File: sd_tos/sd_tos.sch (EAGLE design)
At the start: 18 parts, among them IC1 MEGA16-A, IC3 74HCT595D

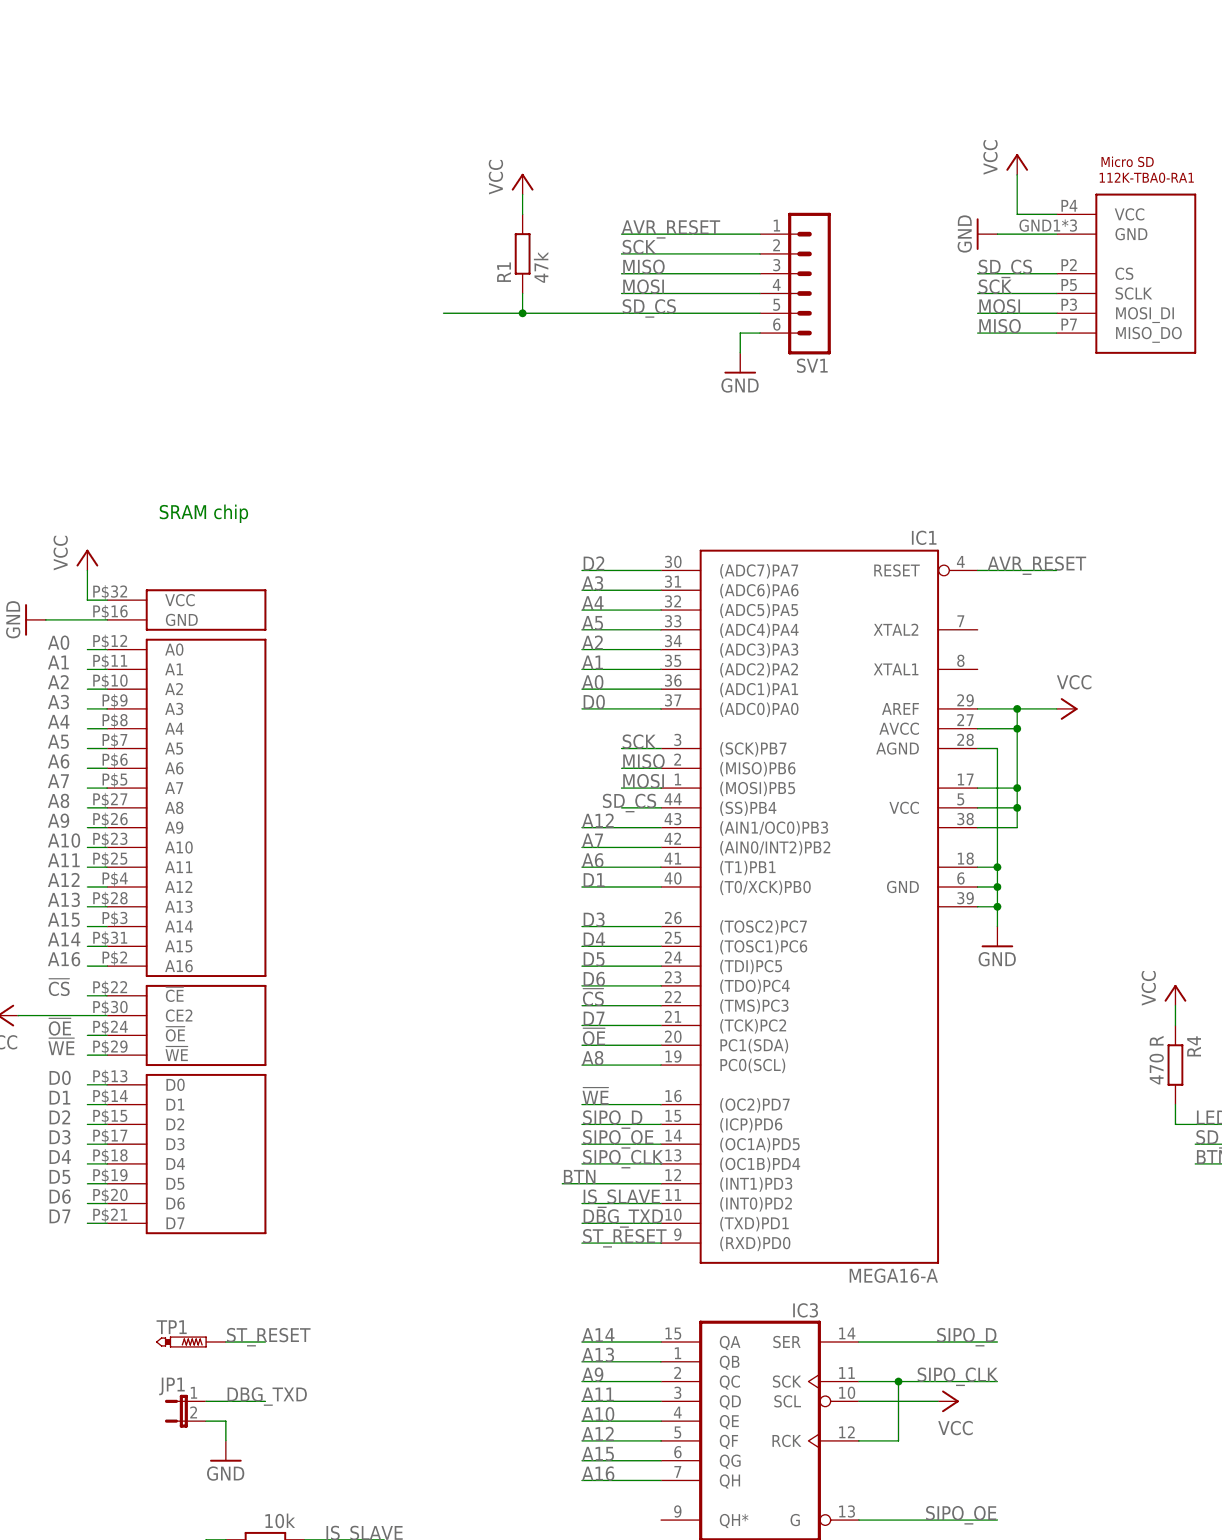
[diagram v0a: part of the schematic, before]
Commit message: added ST reset wire to master/slave connector, so you need to connect only single ST reset wire to the boards and they will share it
git-svn-id: https://subversion.assembla.com/svn/atarijookie/trunk@935 0d2ca917-fb58-4453-bb26-a698c01b0940
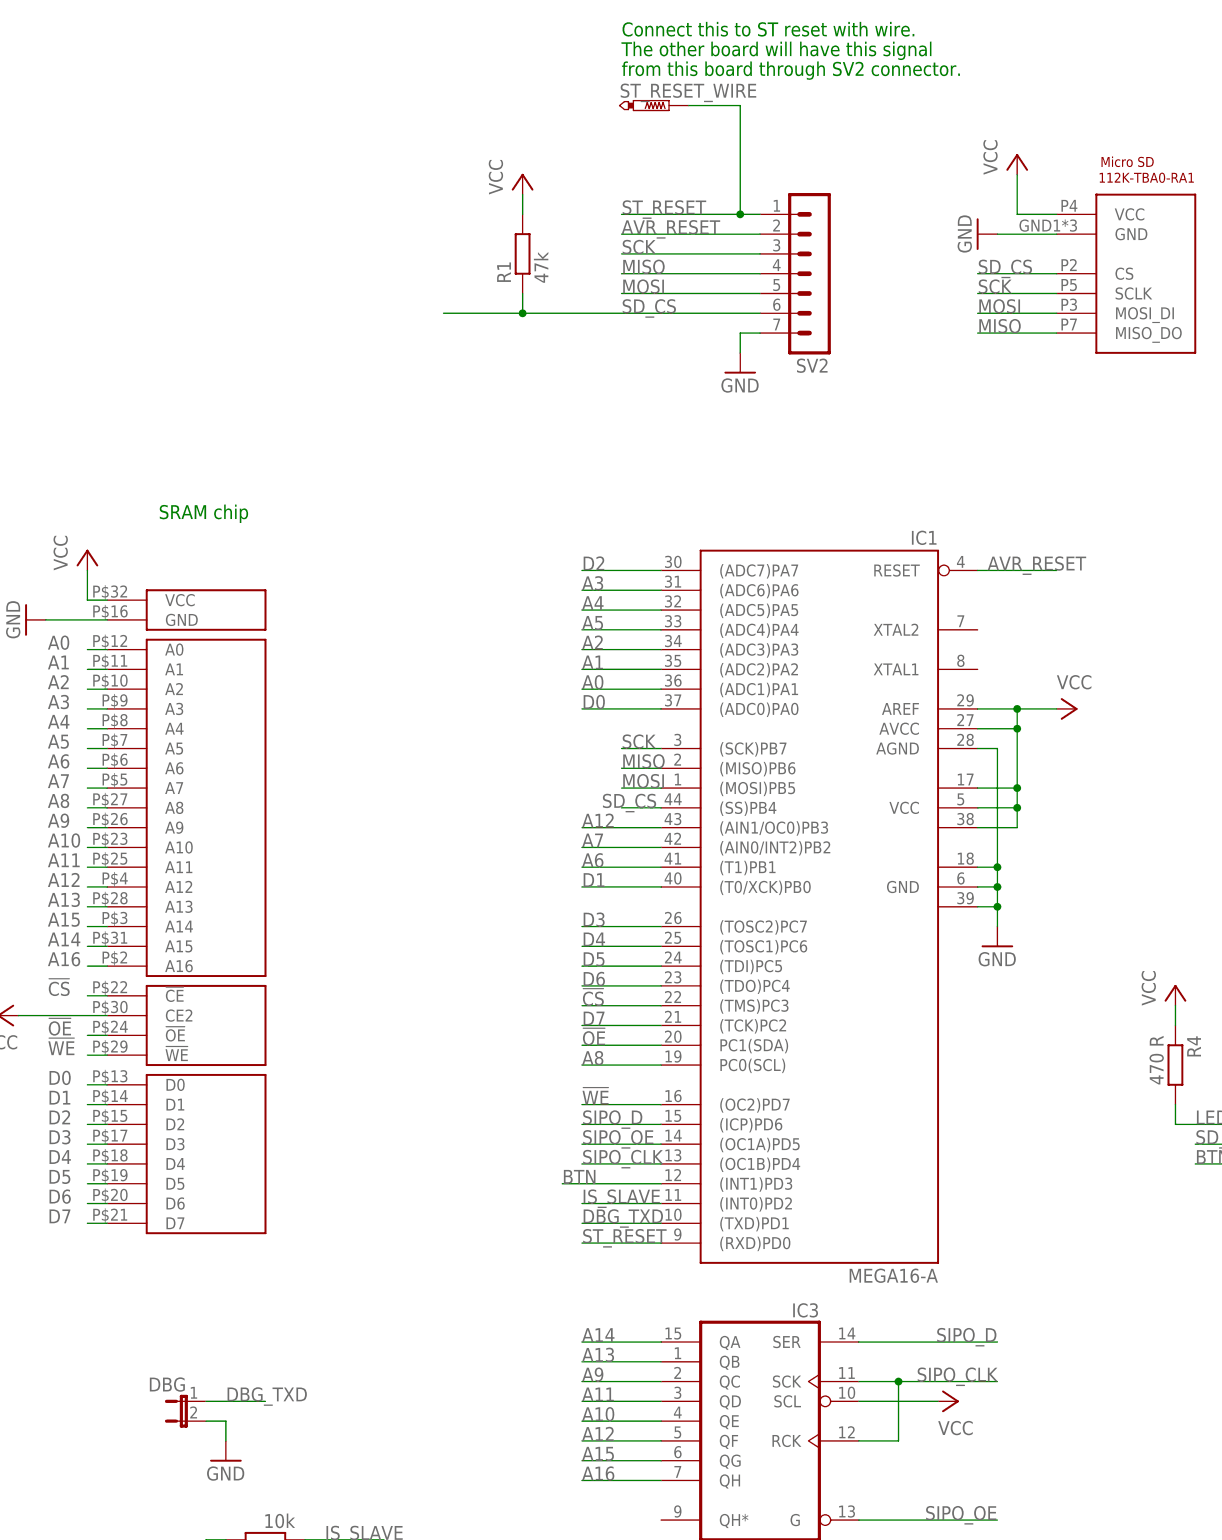
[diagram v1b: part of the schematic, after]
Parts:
- removed SV1: (no value), con-lstb:MA06-1
- removed TP1: PTR1PAD1-13Y, testpad:PTR1PAD1-13Y
- added ST_RESET_WIRE: PTR1PAD1-13Y, testpad:PTR1PAD1-13Y
- added SV2: (no value), con-lstb:MA07-1
- renumbered JP1 to DBG
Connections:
- net AVR_RESET: now also SV2.2; no longer SV1.1
- net GND: now also SV2.7; no longer SV1.6
- net MISO: now also SV2.4; no longer SV1.3
- net MOSI: now also SV2.5; no longer SV1.4
- net SCK: now also SV2.3; no longer SV1.2
- net SD_CS: now also SV2.6; no longer SV1.5
- net ST_RESET: now also ST_RESET_WIRE.TP, SV2.1; no longer TP1.TP
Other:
- note added: "Connect this to ST reset with wire."
- note added: "The other board will have this signal"
- note added: "from this board through SV2 connector."
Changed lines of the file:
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@@
 <setting verticaltext="up"/>
 </settings>
-<grid distance="0.1" unitdist="inch" unit="inch" style="lines" multiple="1" display="no" altdistance="0.05" altunitdist="inch" altunit="inch"/>
+<grid distance="0.1" unitdist="inch" unit="inch" style="lines" multiple="1" display="no" altdistance="0.01" altunitdist="inch" altunit="inch"/>
 <layers>
 <layer number="1" name="Top" color="4" fill="1" visible="no" active="no"/>
@@
 <part name="IC3" library="74xx-eu" deviceset="74*595" device="D" technology="HCT"/>
 <part name="P+5" library="supply1" deviceset="VCC" device=""/>
-<part name="SV1" library="con-lstb" deviceset="MA06-1" device=""/>
 <part name="GND4" library="supply1" deviceset="GND" device=""/>
 <part name="R1" library="rcl" deviceset="R-EU_" device="R0603" value="47k"/>
 <part name="P+7" library="supply1" deviceset="VCC" device=""/>
-<part name="JP1" library="jumper" deviceset="JP1E" device=""/>
+<part name="DBG" library="jumper" deviceset="JP1E" device=""/>
 <part name="GND6" library="supply1" deviceset="GND" device=""/>
-<part name="TP1" library="testpad" deviceset="PTR1" device="PAD1-13Y"/>
+<part name="ST_RESET_WIRE" library="testpad" deviceset="PTR1" device="PAD1-13Y"/>
 <part name="R2" library="rcl" deviceset="R-EU_" device="R0603" value="10k"/>
 <part name="GND7" library="supply1" deviceset="GND" device=""/>
@@
 <part name="R4" library="rcl" deviceset="R-EU_" device="R0603" value="470 R"/>
 <part name="P+9" library="supply1" deviceset="VCC" device=""/>
+<part name="SV2" library="con-lstb" deviceset="MA07-1" device=""/>
 </parts>
 <sheets>
@@
 <text x="99.06" y="-30.48" size="1.778" layer="91">Fit R2 if slave.</text>
 <text x="99.06" y="-33.02" size="1.778" layer="91">NO FIT = master.</text>
+<text x="137.16" y="167.64" size="1.778" layer="91">Connect this to ST reset with wire.</text>
+<text x="137.16" y="165.1" size="1.778" layer="91">The other board will have this signal</text>
+<text x="137.16" y="162.56" size="1.778" layer="91">from this board through SV2 connector.</text>
 </plain>
 <instances>
@@
 <instance part="IC3" gate="P" x="276.86" y="40.64"/>
 <instance part="P+5" gate="VCC" x="180.34" y="-7.62" rot="MR90"/>
-<instance part="SV1" gate="1" x="162.56" y="134.62" rot="R180"/>
 <instance part="GND4" gate="1" x="152.4" y="124.46"/>
 <instance part="R1" gate="G$1" x="124.46" y="139.7" rot="R90"/>
 <instance part="P+7" gate="VCC" x="124.46" y="149.86"/>
-<instance part="JP1" gate="A" x="81.28" y="-7.62" rot="MR270"/>
+<instance part="DBG" gate="A" x="81.28" y="-7.62" rot="MR270"/>
 <instance part="GND6" gate="1" x="86.36" y="-15.24"/>
-<instance part="TP1" gate="G$1" x="83.82" y="0" rot="R270"/>
+<instance part="ST_RESET_WIRE" gate="G$1" x="143.256" y="158.75" rot="R270"/>
 <instance part="R2" gate="G$1" x="91.44" y="-25.4" rot="R180"/>
 <instance part="GND7" gate="1" x="83.82" y="-33.02"/>
@@
 <instance part="R4" gate="G$1" x="208.28" y="35.56" rot="R270"/>
 <instance part="P+9" gate="VCC" x="208.28" y="45.72"/>
+<instance part="SV2" gate="1" x="162.56" y="137.16" rot="R180"/>
 </instances>
 <busses>
@@
 </segment>
 <segment>
-<pinref part="SV1" gate="1" pin="6"/>
 <pinref part="GND4" gate="1" pin="GND"/>
 <wire x1="154.94" y1="129.54" x2="152.4" y2="129.54" width="0.1524" layer="91"/>
 <wire x1="152.4" y1="129.54" x2="152.4" y2="127" width="0.1524" layer="91"/>
-</segment>
-<segment>
-<pinref part="JP1" gate="A" pin="2"/>
+<pinref part="SV2" gate="1" pin="7"/>
+</segment>
+<segment>
+<pinref part="DBG" gate="A" pin="2"/>
 <pinref part="GND6" gate="1" pin="GND"/>
 <wire x1="83.82" y1="-10.16" x2="86.36" y2="-10.16" width="0.1524" layer="91"/>
@@
 </segment>
 <segment>
-<pinref part="SV1" gate="1" pin="2"/>
 <wire x1="154.94" y1="139.7" x2="137.16" y2="139.7" width="0.1524" layer="91"/>
 <label x="137.16" y="139.7" size="1.778" layer="95"/>
+<pinref part="SV2" gate="1" pin="3"/>
 </segment>
 <segment>
@@
 </segment>
 <segment>
-<pinref part="SV1" gate="1" pin="3"/>
 <wire x1="154.94" y1="137.16" x2="137.16" y2="137.16" width="0.1524" layer="91"/>
 <label x="137.16" y="137.16" size="1.778" layer="95"/>
+<pinref part="SV2" gate="1" pin="4"/>
 </segment>
 <segment>
@@
 </segment>
 <segment>
-<pinref part="SV1" gate="1" pin="4"/>
 <wire x1="154.94" y1="134.62" x2="137.16" y2="134.62" width="0.1524" layer="91"/>
 <label x="137.16" y="134.62" size="1.778" layer="95"/>
+<pinref part="SV2" gate="1" pin="5"/>
 </segment>
 <segment>
@@
 </segment>
 <segment>
-<pinref part="SV1" gate="1" pin="1"/>
 <wire x1="154.94" y1="142.24" x2="137.16" y2="142.24" width="0.1524" layer="91"/>
 <label x="137.16" y="142.24" size="1.778" layer="95"/>
+<pinref part="SV2" gate="1" pin="2"/>
 </segment>
 </net>
@@
 </segment>
 <segment>
-<pinref part="JP1" gate="A" pin="1"/>
+<pinref part="DBG" gate="A" pin="1"/>
 <wire x1="83.82" y1="-7.62" x2="91.44" y2="-7.62" width="0.1524" layer="91"/>
 <label x="86.36" y="-7.62" size="1.778" layer="95"/>
@@
 </net>
 <net name="ST_RESET" class="0">
-<segment>
-<pinref part="TP1" gate="G$1" pin="TP"/>
-<wire x1="86.36" y1="0" x2="91.44" y2="0" width="0.1524" layer="91"/>
-<label x="86.36" y="0" size="1.778" layer="95"/>
-</segment>
 <segment>
 <pinref part="IC1" gate="G$1" pin="(RXD)PD0"/>
@@
 <label x="132.08" y="12.7" size="1.778" layer="95"/>
 </segment>
+<segment>
+<pinref part="SV2" gate="1" pin="1"/>
+<wire x1="154.94" y1="144.78" x2="152.4" y2="144.78" width="0.1524" layer="91"/>
+<label x="137.16" y="144.78" size="1.778" layer="95"/>
+<wire x1="152.4" y1="144.78" x2="137.16" y2="144.78" width="0.1524" layer="91"/>
+<wire x1="152.4" y1="144.78" x2="152.4" y2="158.75" width="0.1524" layer="91"/>
+<junction x="152.4" y="144.78"/>
+<pinref part="ST_RESET_WIRE" gate="G$1" pin="TP"/>
+<wire x1="152.4" y1="158.75" x2="145.796" y2="158.75" width="0.1524" layer="91"/>
+</segment>
 </net>
 <net name="IS_SLAVE" class="0">
@@
 <net name="SD_CS" class="0">
 <segment>
-<pinref part="SV1" gate="1" pin="5"/>
 <label x="137.16" y="132.08" size="1.778" layer="95"/>
 <wire x1="154.94" y1="132.08" x2="124.46" y2="132.08" width="0.1524" layer="91"/>
@@
 <wire x1="124.46" y1="134.62" x2="124.46" y2="132.08" width="0.1524" layer="91"/>
 <junction x="124.46" y="132.08"/>
-</segment>
-<segment>
+<pinref part="SV2" gate="1" pin="6"/>
+</segment>
+<segment>

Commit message: activity SMD LED added on PCB - if you don't want to drag the external LED out
git-svn-id: https://subversion.assembla.com/svn/atarijookie/trunk@936 0d2ca917-fb58-4453-bb26-a698c01b0940
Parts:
- added LED_ACT: (no value), led:LEDCHIP-LED0805
- added R5: 470 R, rcl:R-EU_R0603
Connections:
- new net N$2: LED_ACT.A, R5.1
- net SD_CS: now also LED_ACT.C
- net VCC: now also R5.2
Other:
- note added: "AS6C1008"
- moved on the sheet: R1
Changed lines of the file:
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@@
 <part name="P+9" library="supply1" deviceset="VCC" device=""/>
 <part name="SV2" library="con-lstb" deviceset="MA07-1" device=""/>
+<part name="LED_ACT" library="led" deviceset="LED" device="CHIP-LED0805"/>
+<part name="R5" library="rcl" deviceset="R-EU_" device="R0603" value="470 R"/>
+<part name="P+10" library="supply1" deviceset="VCC" device=""/>
 </parts>
 <sheets>
@@
 <text x="137.16" y="165.1" size="1.778" layer="91">The other board will have this signal</text>
 <text x="137.16" y="162.56" size="1.778" layer="91">from this board through SV2 connector.</text>
+<text x="77.724" y="108.458" size="1.778" layer="91">AS6C1008</text>
 </plain>
 <instances>
@@
 <instance part="P+5" gate="VCC" x="180.34" y="-7.62" rot="MR90"/>
 <instance part="GND4" gate="1" x="152.4" y="124.46"/>
-<instance part="R1" gate="G$1" x="124.46" y="139.7" rot="R90"/>
-<instance part="P+7" gate="VCC" x="124.46" y="149.86"/>
+<instance part="R1" gate="G$1" x="124.46" y="154.94" rot="R90"/>
+<instance part="P+7" gate="VCC" x="124.46" y="165.1"/>
 <instance part="DBG" gate="A" x="81.28" y="-7.62" rot="MR270"/>
 <instance part="GND6" gate="1" x="86.36" y="-15.24"/>
@@
 <instance part="P+9" gate="VCC" x="208.28" y="45.72"/>
 <instance part="SV2" gate="1" x="162.56" y="137.16" rot="R180"/>
+<instance part="LED_ACT" gate="G$1" x="111.76" y="142.24"/>
+<instance part="R5" gate="G$1" x="111.76" y="154.94" rot="R90"/>
+<instance part="P+10" gate="VCC" x="111.76" y="165.1"/>
 </instances>
 <busses>
@@
 <pinref part="R1" gate="G$1" pin="2"/>
 <pinref part="P+7" gate="VCC" pin="VCC"/>
-<wire x1="124.46" y1="144.78" x2="124.46" y2="147.32" width="0.1524" layer="91"/>
+<wire x1="124.46" y1="160.02" x2="124.46" y2="162.56" width="0.1524" layer="91"/>
 </segment>
 <segment>
@@
 <pinref part="R4" gate="G$1" pin="1"/>
 <wire x1="208.28" y1="43.18" x2="208.28" y2="40.64" width="0.1524" layer="91"/>
+</segment>
+<segment>
+<pinref part="P+10" gate="VCC" pin="VCC"/>
+<pinref part="R5" gate="G$1" pin="2"/>
+<wire x1="111.76" y1="162.56" x2="111.76" y2="160.02" width="0.1524" layer="91"/>
 </segment>
 </net>
@@
 <wire x1="154.94" y1="132.08" x2="124.46" y2="132.08" width="0.1524" layer="91"/>
 <pinref part="R1" gate="G$1" pin="1"/>
-<wire x1="124.46" y1="132.08" x2="114.3" y2="132.08" width="0.1524" layer="91"/>
-<wire x1="124.46" y1="134.62" x2="124.46" y2="132.08" width="0.1524" layer="91"/>
+<wire x1="124.46" y1="132.08" x2="111.76" y2="132.08" width="0.1524" layer="91"/>
+<wire x1="124.46" y1="149.86" x2="124.46" y2="132.08" width="0.1524" layer="91"/>
 <junction x="124.46" y="132.08"/>
 <pinref part="SV2" gate="1" pin="6"/>
+<pinref part="LED_ACT" gate="G$1" pin="C"/>
+<wire x1="111.76" y1="137.16" x2="111.76" y2="132.08" width="0.1524" layer="91"/>
+<wire x1="111.76" y1="132.08" x2="104.14" y2="132.08" width="0.1524" layer="91"/>
+<junction x="111.76" y="132.08"/>
 </segment>
 <segment>
@@
 </segment>
 </net>
+<net name="N$2" class="0">
+<segment>
+<pinref part="R5" gate="G$1" pin="1"/>
+<pinref part="LED_ACT" gate="G$1" pin="A"/>
+<wire x1="111.76" y1="149.86" x2="111.76" y2="144.78" width="0.1524" layer="91"/>
+</segment>
+</net>
